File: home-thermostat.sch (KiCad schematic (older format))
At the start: 13 parts

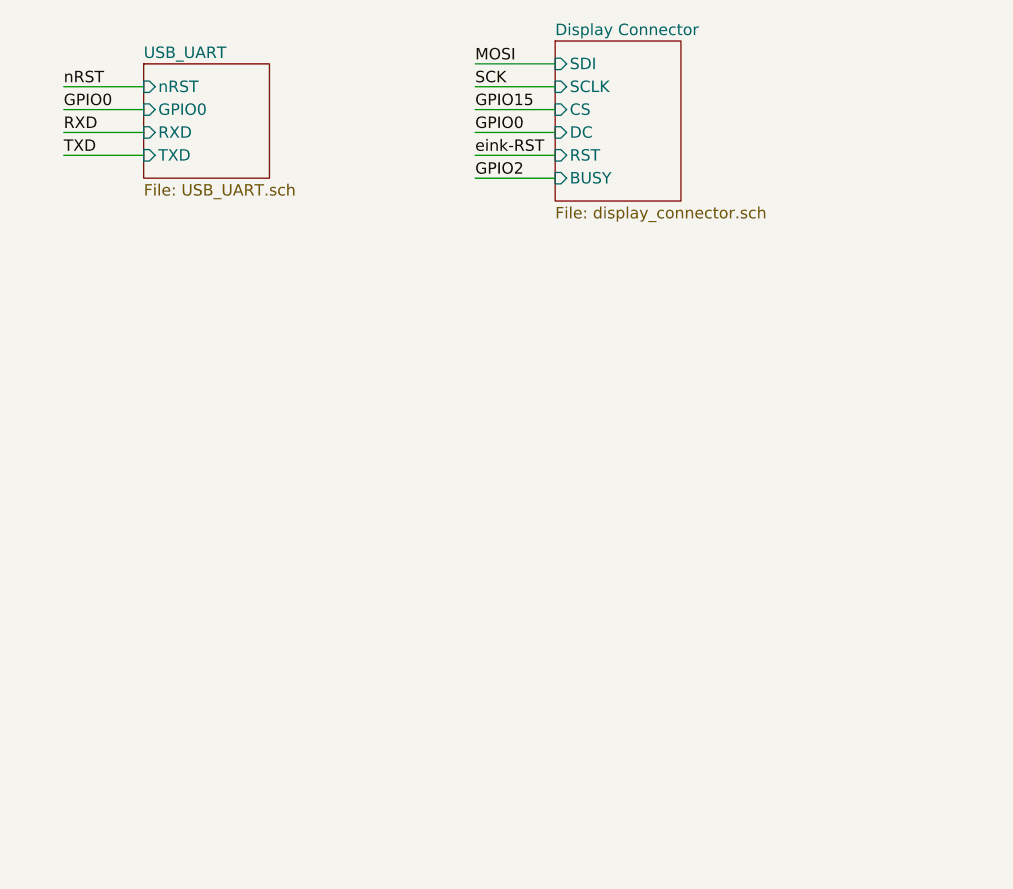
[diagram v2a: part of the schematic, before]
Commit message: Changed usb port to ISP programming as CP2102 IC is not available from Reichelt.
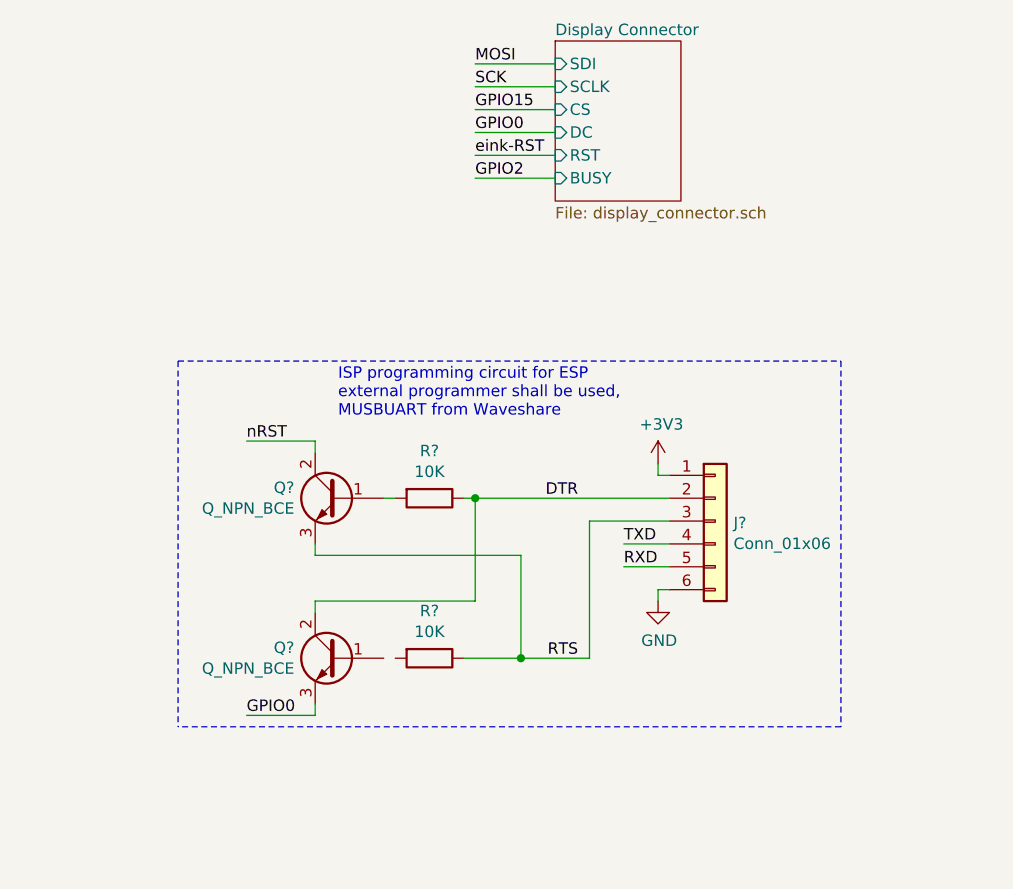
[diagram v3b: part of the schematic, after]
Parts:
- added J?: Conn_01x06, symbol Connector_Generic:Conn_01x06
- added Q? (x2): Q_NPN_BCE, symbol Device:Q_NPN_BCE
- added R? (x2): 10K, symbol Device:R
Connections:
- net labels added: DTR, RTS
- wire segments 68 -> 87
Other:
- note added: "ISP programming circuit for ESP\nexternal programmer shall be used,\nMUSBUART from Waveshare"
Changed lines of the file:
@@
 $Descr A4 11693 8268
 encoding utf-8
-Sheet 1 5
+Sheet 1 4
 Title ""
 Date ""
@@
 Wire Wire Line
 	4700 5700 4500 5700
-$Sheet
-S 1250 1000 550  500
-U 5E62DF31
-F0 "USB_UART" 50
-F1 "USB_UART.sch" 50
-F2 "nRST" I L 1250 1100 50
-F3 "GPIO0" I L 1250 1200 50
-F4 "RXD" I L 1250 1300 50
-F5 "TXD" I L 1250 1400 50
-$EndSheet
 $Sheet
 S 3050 900  550  700
@@
 F7 "BUSY" I L 3050 1500 50
 $EndSheet
-Text Label 900  1100 0    50   ~ 0
-nRST
-Text Label 900  1200 0    50   ~ 0
-GPIO0
-Text Label 900  1300 0    50   ~ 0
-RXD
-Text Label 900  1400 0    50   ~ 0
-TXD
-Wire Wire Line
-	900  1100 1250 1100
-Wire Wire Line
-	900  1200 1250 1200
-Wire Wire Line
-	900  1300 1250 1300
-Wire Wire Line
-	900  1400 1250 1400
 Text Label 2700 1200 0    50   ~ 0
 GPIO15
@@
 Text Notes 8800 4400 0    50   ~ 0
 Maybe use goldcap?
+$Comp
+L Device:Q_NPN_BCE Q?
+U 1 1 5E94DFC6
+P 2100 2900
+AR Path="/5E94DFC6" Ref="Q?"  Part="1"
+AR Path="/5E62DF31/5E94DFC6" Ref="Q?"  Part="1"
+F 0 "Q?" H 2291 2946 50  0000 L CNN
+F 1 "Q_NPN_BCE" H 2291 2855 50  0000 L CNN
+F 2 "" H 2300 3000 50  0001 C CNN
+F 3 "~" H 2100 2900 50  0001 C CNN
+	1    2100 2900
+	-1   0    0    -1
+$EndComp
+$Comp
+L Device:Q_NPN_BCE Q?
+U 1 1 5E94DFCC
+P 2100 3600
+AR Path="/5E94DFCC" Ref="Q?"  Part="1"
+AR Path="/5E62DF31/5E94DFCC" Ref="Q?"  Part="1"
+F 0 "Q?" H 2291 3646 50  0000 L CNN
+F 1 "Q_NPN_BCE" H 2291 3555 50  0000 L CNN
+F 2 "" H 2300 3700 50  0001 C CNN
+F 3 "~" H 2100 3600 50  0001 C CNN
+	1    2100 3600
+	-1   0    0    -1
+$EndComp
+$Comp
+L Device:R R?
+U 1 1 5E94DFD2
+P 2500 2900
+AR Path="/5E94DFD2" Ref="R?"  Part="1"
+AR Path="/5E62DF31/5E94DFD2" Ref="R?"  Part="1"
+F 0 "R?" V 2293 2900 50  0000 C CNN
+F 1 "10K" V 2384 2900 50  0000 C CNN
+F 2 "" V 2430 2900 50  0001 C CNN
+F 3 "~" H 2500 2900 50  0001 C CNN
+	1    2500 2900
+	0    1    1    0
+$EndComp
+$Comp
+L Device:R R?
+U 1 1 5E94DFD8
+P 2500 3600
+AR Path="/5E94DFD8" Ref="R?"  Part="1"
+AR Path="/5E62DF31/5E94DFD8" Ref="R?"  Part="1"
+F 0 "R?" V 2293 3600 50  0000 C CNN
+F 1 "10K" V 2384 3600 50  0000 C CNN
+F 2 "" V 2430 3600 50  0001 C CNN
+F 3 "~" H 2500 3600 50  0001 C CNN
+	1    2500 3600
+	0    1    1    0
+$EndComp
+Wire Wire Line
+	2350 2900 2300 2900
+Wire Wire Line
+	2000 3100 2000 3150
+Wire Wire Line
+	2000 3350 2000 3400
+Wire Wire Line
+	2650 2900 2700 2900
+Wire Wire Line
+	2700 3350 2700 2900
+Wire Wire Line
+	2000 3350 2700 3350
+Connection ~ 2700 2900
+Wire Wire Line
+	2650 3600 2900 3600
+Wire Wire Line
+	2900 3150 2900 3600
+Wire Wire Line
+	2000 3150 2900 3150
+Connection ~ 2900 3600
+Wire Wire Line
+	2000 2700 2000 2650
+Wire Wire Line
+	2000 2650 1700 2650
+Wire Wire Line
+	2000 3800 2000 3850
+Wire Wire Line
+	2000 3850 1700 3850
+Text Label 3150 2900 2    50   ~ 0
+DTR
+Text Label 3150 3600 2    50   ~ 0
+RTS
+Text Label 1700 2650 0    50   ~ 0
+nRST
+Text Label 1700 3850 0    50   ~ 0
+GPIO0
+$Comp
+L Connector_Generic:Conn_01x06 J?
+U 1 1 5E95132C
+P 3750 3000
+F 0 "J?" H 3830 2992 50  0000 L CNN
+F 1 "Conn_01x06" H 3830 2901 50  0000 L CNN
+F 2 "" H 3750 3000 50  0001 C CNN
+F 3 "~" H 3750 3000 50  0001 C CNN
+	1    3750 3000
+	1    0    0    -1
+$EndComp
+$Comp
+L power:GND #PWR?
+U 1 1 5E951C47
+P 3500 3350
+F 0 "#PWR?" H 3500 3100 50  0001 C CNN
+F 1 "GND" H 3505 3177 50  0000 C CNN
+F 2 "" H 3500 3350 50  0001 C CNN
+F 3 "" H 3500 3350 50  0001 C CNN
+	1    3500 3350
+	1    0    0    -1
+$EndComp
+Wire Wire Line
+	3500 3350 3500 3300
+Wire Wire Line
+	3500 3300 3550 3300
+$Comp
+L power:+3V3 #PWR?
+U 1 1 5E954243
+P 3500 2750
+F 0 "#PWR?" H 3500 2600 50  0001 C CNN
+F 1 "+3V3" H 3515 2923 50  0000 C CNN
+F 2 "" H 3500 2750 50  0001 C CNN
+F 3 "" H 3500 2750 50  0001 C CNN
+	1    3500 2750
+	1    0    0    -1
+$EndComp
+Wire Wire Line
+	3500 2750 3500 2800
+Wire Wire Line
+	3500 2800 3550 2800
+Text Label 3350 3200 0    50   ~ 0
+RXD
+Wire Wire Line
+	3350 3200 3550 3200
+Text Label 3350 3100 0    50   ~ 0
+TXD
+Wire Wire Line
+	3350 3100 3550 3100
+Wire Wire Line
+	2700 2900 3550 2900
+Wire Wire Line
+	3200 3600 3200 3000
+Wire Wire Line
+	3200 3000 3550 3000
+Wire Wire Line
+	2900 3600 3200 3600
+Text Notes 2100 2550 0    50   ~ 0
+ISP programming circuit for ESP\nexternal programmer shall be used,\nMUSBUART from Waveshare
+Wire Notes Line
+	1400 2300 4300 2300
+Wire Notes Line
+	4300 2300 4300 3900
+Wire Notes Line
+	4300 3900 1400 3900
+Wire Notes Line
+	1400 2300 1400 3900
 $EndSCHEMATC

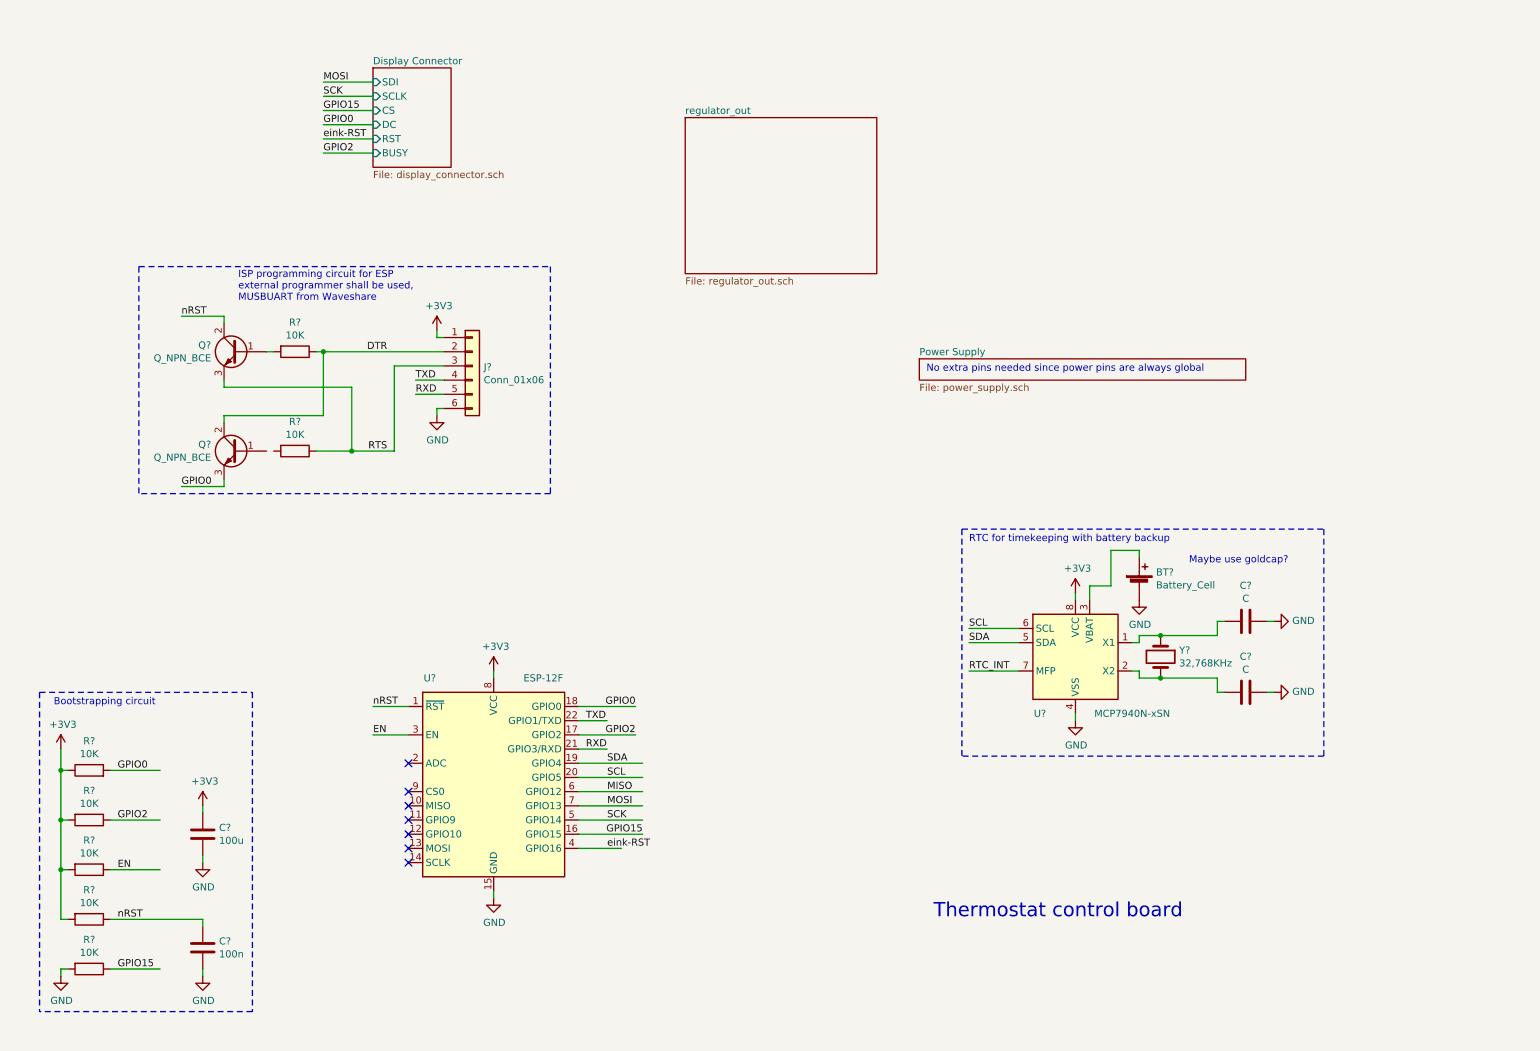
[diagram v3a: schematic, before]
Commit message: Added Temperature sensor.
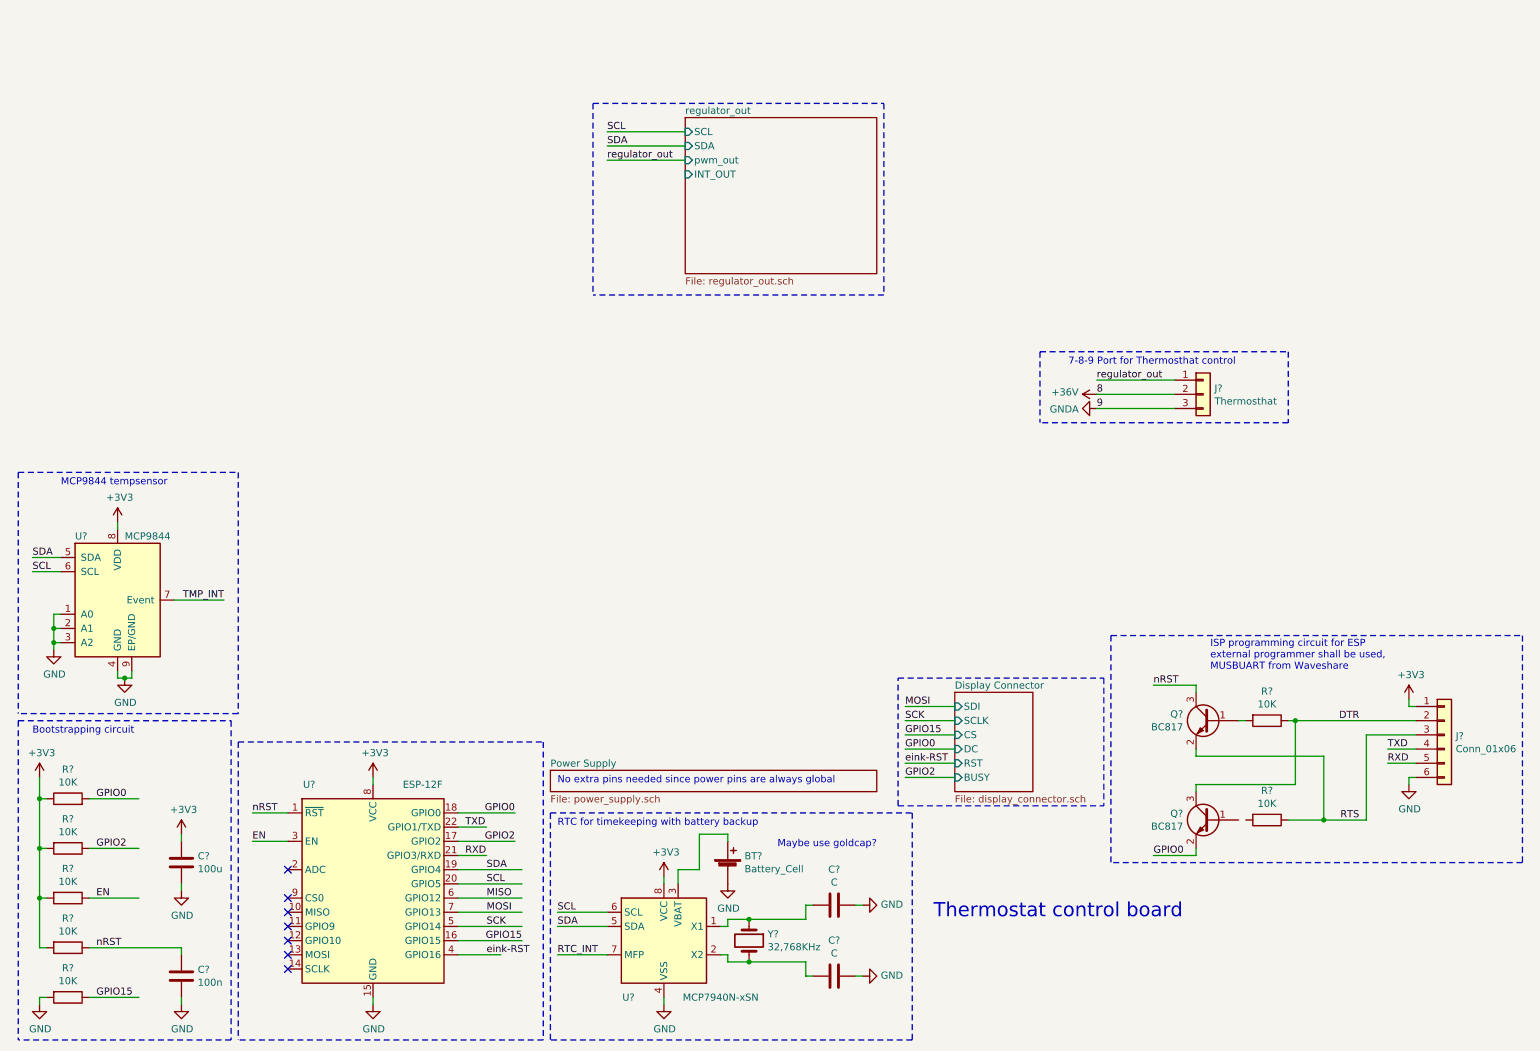
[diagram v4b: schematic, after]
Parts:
- removed Q? (x2): Q_NPN_BCE, symbol Device:Q_NPN_BCE
- added J?: Thermosthat, symbol Connector_Generic:Conn_01x03
- added Q? (x2): BC817, symbol Device:Q_NPN_BEC
- added U?: MCP9844, Package_DFN_QFN:DFN-8-1EP_3x2mm_P0.5mm_EP1.36x1.46mm, symbol Sensor_Temperature:MCP9844
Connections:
- net labels added: +36V, 8, 9, GNDA, TMP_INT, regulator_out
- wire segments 87 -> 107
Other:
- note added: "7-8-9 Port for Thermosthat control"
- note added: "MCP9844 tempsensor"
- moved on the sheet: BT?, C?, J?, R?, U?, Y?

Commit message: Initial draft of thermostat done, beautified circuit diagram.
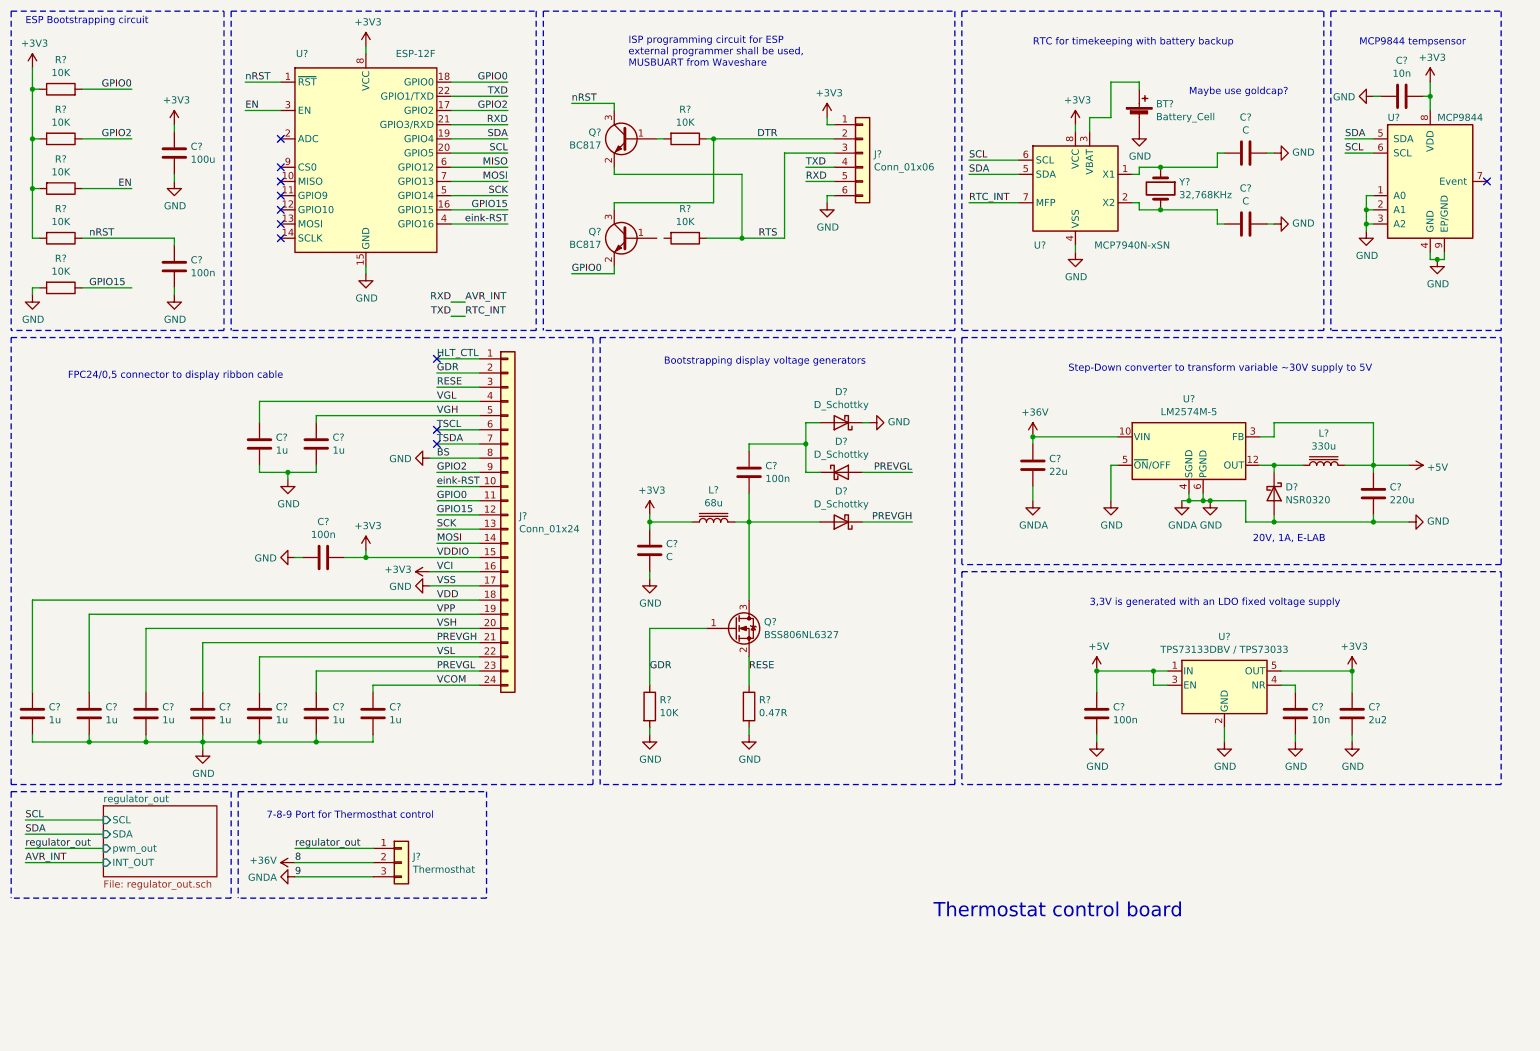
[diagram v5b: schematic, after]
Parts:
- added C?: 22u, symbol Device:C
- added C?: 220u, symbol Device:C
- added C? (x3): 100n, symbol Device:C
- added C? (x2): 10n, symbol Device:C
- added C?: 2u2, symbol Device:C
- added C? (x9): 1u, symbol Device:C
- added C?: C, symbol Device:C
- added D?: NSR0320, symbol Device:D_Schottky
- added D? (x3): D_Schottky, symbol Device:D_Schottky
- added J?: Conn_01x24, symbol Connector_Generic:Conn_01x24
- added L?: 330u, symbol Device:L_Core_Iron
- added L?: 68u, symbol Device:L_Core_Iron
- added Q?: BSS806NL6327, symbol Device:Q_NMOS_GSD
- added R?: 10K, symbol Device:R
- added R?: 0.47R, symbol Device:R
- added U?: LM2574M-5, Package_SO:SOIC-14W_7.5x9mm_P1.27mm, symbol Regulator_Switching:LM2574M-5
- added U?: TPS73133DBV / TPS73033, Package_TO_SOT_SMD:SOT-23-5, symbol Regulator_Linear:TPS73133DBV
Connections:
- net labels added: +5V, AVR_INT, BS, GDR, HLT_CTL, PREVGH, PREVGL, RESE, TSCL, TSDA, VCI, VCOM, VDD, VDDIO, VGH, VGL, VPP, VSH, VSL, VSS
- net labels removed: TMP_INT
- wire segments 107 -> 223
- no-connect marks 7 -> 11
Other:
- note added: "20V, 1A, E-LAB"
- note added: "3,3V is generated with an LDO fixed voltage supply"
- note added: "Bootstrapping display voltage generators"
- note added: "ESP Bootstrapping circuit"
- note added: "FPC24/0,5 connector to display ribbon cable"
- note added: "Step-Down converter to transform variable ~~30V supply to 5V"
- note removed: "Bootstrapping circuit"
- note removed: "No extra pins needed since power pins are always global"
- moved on the sheet: BT?, C?, J?, Q?, R?, U?, Y?
